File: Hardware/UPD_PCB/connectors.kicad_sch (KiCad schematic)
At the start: 23 parts, among them J1 Screw_Terminal_01x02, J10 Screw_Terminal_01x02, J2 Screw_Terminal_01x02, J3 Screw_Terminal_01x02, J4 Screw_Terminal_01x02, J5 Screw_Terminal_01x02, J6 Screw_Terminal_01x02, J7 Screw_Terminal_01x02, J8 Screw_Terminal_01x02, J9 Screw_Terminal_01x02

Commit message: Updated design
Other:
- moved on the sheet: J3, J4
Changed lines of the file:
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@@
 	(wire
 		(pts
-			(xy 63.5 45.72) (xy 69.85 45.72)
+			(xy 59.69 45.72) (xy 66.04 45.72)
 		)
 		(stroke
@@
 	(wire
 		(pts
-			(xy 63.5 62.23) (xy 66.04 62.23)
+			(xy 59.69 62.23) (xy 62.23 62.23)
 		)
 		(stroke
@@
 	(wire
 		(pts
-			(xy 63.5 59.69) (xy 66.04 59.69)
+			(xy 59.69 59.69) (xy 62.23 59.69)
 		)
 		(stroke
@@
 	(wire
 		(pts
-			(xy 66.04 48.26) (xy 63.5 48.26)
+			(xy 62.23 48.26) (xy 59.69 48.26)
 		)
 		(stroke
@@
 	)
 	(label "IP+"
-		(at 69.85 45.72 180)
+		(at 66.04 45.72 180)
 		(fields_autoplaced yes)
 		(effects
@@
 	(symbol
 		(lib_id "Connector:Screw_Terminal_01x02")
-		(at 58.42 62.23 180)
+		(at 54.61 62.23 180)
 		(unit 1)
 		(exclude_from_sim no)
@@
 		(dnp no)
 		(property "Reference" "J4"
-			(at 56.388 62.484 0)
+			(at 52.578 62.484 0)
 			(effects
 				(font
@@
 		)
 		(property "Value" "Screw_Terminal_01x02"
-			(at 56.388 59.944 0)
+			(at 52.578 59.944 0)
 			(effects
 				(font
@@
 		)
 		(property "Footprint" ""
-			(at 58.42 62.23 0)
+			(at 54.61 62.23 0)
 			(effects
 				(font
@@
 		)
 		(property "Datasheet" "~"
-			(at 58.42 62.23 0)
+			(at 54.61 62.23 0)
 			(effects
 				(font
@@
 		)
 		(property "Description" "Generic screw terminal, single row, 01x02, script generated (kicad-library-utils/schlib/autogen/connector/)"
-			(at 58.42 62.23 0)
+			(at 54.61 62.23 0)
 			(effects
 				(font
@@
 	(symbol
 		(lib_id "power:GND")
-		(at 66.04 62.23 0)
+		(at 62.23 62.23 0)
 		(unit 1)
 		(exclude_from_sim no)
@@
 		(fields_autoplaced yes)
 		(property "Reference" "#PWR058"
-			(at 66.04 68.58 0)
+			(at 62.23 68.58 0)
 			(effects
 				(font
@@
 		)
 		(property "Value" "GND"
-			(at 66.04 67.31 0)
+			(at 62.23 67.31 0)
 			(effects
 				(font
@@
 		)
 		(property "Footprint" ""
-			(at 66.04 62.23 0)
+			(at 62.23 62.23 0)
 			(effects
 				(font
@@
 		)
 		(property "Datasheet" ""
-			(at 66.04 62.23 0)
+			(at 62.23 62.23 0)
 			(effects
 				(font
@@
 		)
 		(property "Description" "Power symbol creates a global label with name \"GND\" , ground"
-			(at 66.04 62.23 0)
+			(at 62.23 62.23 0)
 			(effects
 				(font
@@
 	(symbol
 		(lib_id "power:GND")
-		(at 66.04 48.26 0)
+		(at 62.23 48.26 0)
 		(unit 1)
 		(exclude_from_sim no)
@@
 		(fields_autoplaced yes)
 		(property "Reference" "#PWR056"
-			(at 66.04 54.61 0)
+			(at 62.23 54.61 0)
 			(effects
 				(font
@@
 		)
 		(property "Value" "GND"
-			(at 66.04 53.34 0)
+			(at 62.23 53.34 0)
 			(effects
 				(font
@@
 		)
 		(property "Footprint" ""
-			(at 66.04 48.26 0)
+			(at 62.23 48.26 0)
 			(effects
 				(font
@@
 		)
 		(property "Datasheet" ""
-			(at 66.04 48.26 0)
+			(at 62.23 48.26 0)
 			(effects
 				(font
@@
 		)
 		(property "Description" "Power symbol creates a global label with name \"GND\" , ground"
-			(at 66.04 48.26 0)
+			(at 62.23 48.26 0)
 			(effects
 				(font
@@
 	(symbol
 		(lib_id "Connector:Screw_Terminal_01x02")
-		(at 58.42 48.26 180)
+		(at 54.61 48.26 180)
 		(unit 1)
 		(exclude_from_sim no)
@@
 		(dnp no)
 		(property "Reference" "J3"
-			(at 56.388 48.514 0)
+			(at 52.578 48.514 0)
 			(effects
 				(font
@@
 		)
 		(property "Value" "Screw_Terminal_01x02"
-			(at 56.388 45.974 0)
+			(at 52.578 45.974 0)
 			(effects
 				(font
@@
 		)
 		(property "Footprint" ""
-			(at 58.42 48.26 0)
+			(at 54.61 48.26 0)
 			(effects
 				(font
@@
 		)
 		(property "Datasheet" "~"
-			(at 58.42 48.26 0)
+			(at 54.61 48.26 0)
 			(effects
 				(font
@@
 		)
 		(property "Description" "Generic screw terminal, single row, 01x02, script generated (kicad-library-utils/schlib/autogen/connector/)"
-			(at 58.42 48.26 0)
+			(at 54.61 48.26 0)
 			(effects
 				(font
@@
 	(symbol
 		(lib_id "power:+5V")
-		(at 66.04 59.69 270)
+		(at 62.23 59.69 270)
 		(unit 1)
 		(exclude_from_sim no)
@@
 		(fields_autoplaced yes)
 		(property "Reference" "#PWR057"
+			(at 58.42 59.69 0)
+			(effects
+				(font
+					(size 1.27 1.27)
+				)
+				(hide yes)
+			)
+		)
+		(property "Value" "+5V"
+			(at 66.04 59.6899 90)
+			(effects
+				(font
+					(size 1.27 1.27)
+				)
+				(justify left)
+			)
+		)
+		(property "Footprint" ""
 			(at 62.23 59.69 0)
 			(effects
@@
 			)
 		)
-		(property "Value" "+5V"
-			(at 69.85 59.6899 90)
-			(effects
-				(font
-					(size 1.27 1.27)
-				)
-				(justify left)
-			)
-		)
-		(property "Footprint" ""
-			(at 66.04 59.69 0)
-			(effects
-				(font
-					(size 1.27 1.27)
-				)
-				(hide yes)
-			)
-		)
 		(property "Datasheet" ""
-			(at 66.04 59.69 0)
+			(at 62.23 59.69 0)
 			(effects
 				(font
@@
 		)
 		(property "Description" "Power symbol creates a global label with name \"+5V\""
-			(at 66.04 59.69 0)
-			(effects
-				(font
+			(at 62.23 59.69 0)
+			(effects
+				(font

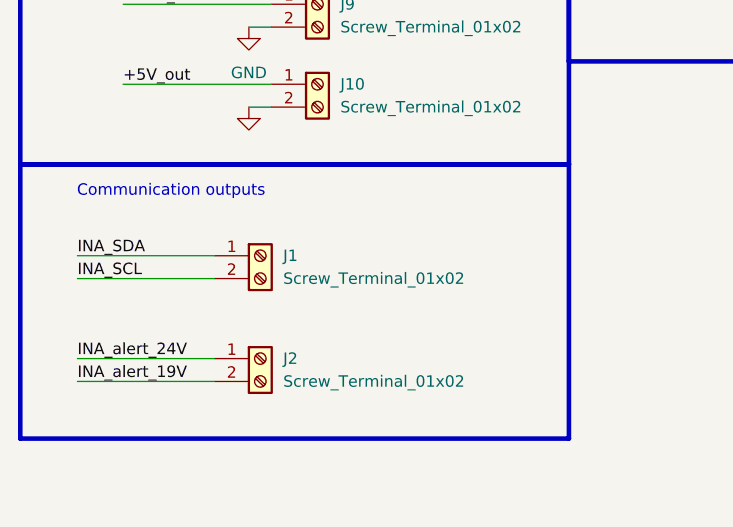
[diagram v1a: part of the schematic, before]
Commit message: Updated schematic (before INA219 integration)
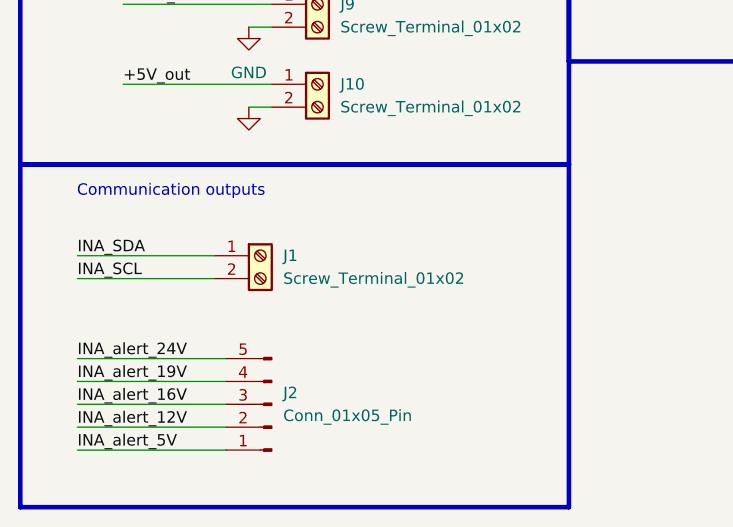
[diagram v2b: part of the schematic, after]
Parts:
- removed J2: Screw_Terminal_01x02, symbol Connector:Screw_Terminal_01x02
- added J2: Conn_01x05_Pin, Connector_PinHeader_1.00mm:PinHeader_1x05_P1.00mm_Vertical, symbol Connector:Conn_01x05_Pin
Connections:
- net INA_alert_19V: now also J2.4 (Pin_4)
- net INA_alert_24V: now also J2.5 (Pin_5)
- new net INA_alert_12V: J2.2 (Pin_2)
- new net INA_alert_16V: J2.3 (Pin_3)
- new net INA_alert_5V: J2.1 (Pin_1)
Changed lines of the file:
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@@
+	(wire
+		(pts
+			(xy 33.02 166.37) (xy 49.53 166.37)
+		)
+		(stroke
+			(width 0)
+			(type default)
+		)
+	)
 	(wire
 		(pts
@@
 	(wire
 		(pts
-			(xy 33.02 158.75) (xy 48.26 158.75)
+			(xy 33.02 158.75) (xy 49.53 158.75)
+		)
+		(stroke
+			(width 0)
+			(type default)
+		)
+	)
+	(wire
+		(pts
+			(xy 33.02 163.83) (xy 49.53 163.83)
 		)
 		(stroke
@@
 	(wire
 		(pts
-			(xy 33.02 161.29) (xy 48.26 161.29)
+			(xy 33.02 161.29) (xy 49.53 161.29)
 		)
 		(stroke
@@
 		(pts
 			(xy 93.98 43.18) (xy 104.14 43.18)
+		)
+		(stroke
+			(width 0)
+			(type default)
+		)
+	)
+	(wire
+		(pts
+			(xy 33.02 168.91) (xy 49.53 168.91)
 		)
 		(stroke
@@
 	(rectangle
 		(start 26.67 137.16)
-		(end 87.63 167.64)
+		(end 87.63 175.26)
 		(stroke
 			(width 0.508)
@@
 		)
 	)
+	(label "INA_alert_5V"
+		(at 33.02 168.91 0)
+		(fields_autoplaced yes)
+		(effects
+			(font
+				(size 1.27 1.27)
+			)
+			(justify left bottom)
+		)
+	)
 	(label "INA_SDA"
 		(at 33.02 147.32 0)
@@
 		)
 	)
+	(label "INA_alert_12V"
+		(at 33.02 166.37 0)
+		(fields_autoplaced yes)
+		(effects
+			(font
+				(size 1.27 1.27)
+			)
+			(justify left bottom)
+		)
+	)
 	(label "+12V_out"
 		(at 93.98 91.44 0)
@@
 		)
 	)
+	(label "INA_alert_16V"
+		(at 33.02 163.83 0)
+		(fields_autoplaced yes)
+		(effects
+			(font
+				(size 1.27 1.27)
+			)
+			(justify left bottom)
+		)
+	)
 	(label "IP+"
 		(at 66.04 45.72 180)
@@
 	)
 	(symbol
-		(lib_id "Connector:Screw_Terminal_01x02")
-		(at 53.34 158.75 0)
-		(unit 1)
-		(exclude_from_sim no)
-		(in_bom yes)
-		(on_board yes)
-		(dnp no)
-		(fields_autoplaced yes)
-		(property "Reference" "J2"
-			(at 55.88 158.7499 0)
-			(effects
-				(font
-					(size 1.27 1.27)
-				)
-				(justify left)
-			)
-		)
-		(property "Value" "Screw_Terminal_01x02"
-			(at 55.88 161.2899 0)
-			(effects
-				(font
-					(size 1.27 1.27)
-				)
-				(justify left)
-			)
-		)
-		(property "Footprint" ""
-			(at 53.34 158.75 0)
-			(effects
-				(font
-					(size 1.27 1.27)
-				)
-				(hide yes)
-			)
-		)
-		(property "Datasheet" "~"
-			(at 53.34 158.75 0)
-			(effects
-				(font
-					(size 1.27 1.27)
-				)
-				(hide yes)
-			)
-		)
-		(property "Description" "Generic screw terminal, single row, 01x02, script generated (kicad-library-utils/schlib/autogen/connector/)"
-			(at 53.34 158.75 0)
-			(effects
-				(font
-					(size 1.27 1.27)
-				)
-				(hide yes)
-			)
-		)
-		(pin "2"
-		)
-		(pin "1"
-		)
-		(instances
-			(project "UPD_PCB"
-				(path "/0650c7a8-acba-429c-9f8e-eec0baf0bc1c/fede4c36-00cc-4d3d-b71c-5243ba232202/7d5a1283-086b-46b0-8df7-a9850521fb5e/4a3b49c6-ce69-4997-95b2-b7bb4e96c397"
-					(reference "J2")
-					(unit 1)
-				)
-			)
-		)
-	)
-	(symbol
 		(lib_id "Device:LED")
 		(at 107.95 80.01 180)
@@
 					(unit 1)
 				)
+			)
+		)
+	)
+	(symbol
+		(lib_id "Connector:Conn_01x05_Pin")
+		(at 54.61 163.83 180)
+		(unit 1)
+		(exclude_from_sim no)
+		(in_bom yes)
+		(on_board yes)
+		(dnp no)
+		(fields_autoplaced yes)
+		(property "Reference" "J2"
+			(at 55.88 162.5599 0)
+			(effects
+				(font
+					(size 1.27 1.27)
+				)
+				(justify right)
+			)
+		)
+		(property "Value" "Conn_01x05_Pin"
+			(at 55.88 165.0999 0)
+			(effects
+				(font
+					(size 1.27 1.27)
+				)
+				(justify right)
+			)
+		)
+		(property "Footprint" "Connector_PinHeader_1.00mm:PinHeader_1x05_P1.00mm_Vertical"
+			(at 54.61 163.83 0)
+			(effects
+				(font
+					(size 1.27 1.27)
+				)
+				(hide yes)
+			)
+		)
+		(property "Datasheet" "~"
+			(at 54.61 163.83 0)
+			(effects
+				(font
+					(size 1.27 1.27)
+				)
+				(hide yes)
+			)
+		)
+		(property "Description" "Generic connector, single row, 01x05, script generated"
+			(at 54.61 163.83 0)
+			(effects
+				(font
+					(size 1.27 1.27)
+				)
+				(hide yes)
+			)
+		)
+		(pin "1"
+		)
+		(pin "4"
+		)
+		(pin "3"
+		)
+		(pin "2"
+		)
+		(pin "5"
+		)
+		(instances
+			(project ""
+				(path "/0650c7a8-acba-429c-9f8e-eec0baf0bc1c/fede4c36-00cc-4d3d-b71c-5243ba232202/7d5a1283-086b-46b0-8df7-a9850521fb5e/4a3b49c6-ce69-4997-95b2-b7bb4e96c397"
+					(reference "J2")
+					(unit 1)
+				)

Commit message: Finalized Schematic
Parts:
- removed F1: Fuse, symbol Device:Fuse
- removed J1: Screw_Terminal_01x02, symbol Connector:Screw_Terminal_01x02
- removed J2: Conn_01x05_Pin, Connector_PinHeader_1.00mm:PinHeader_1x05_P1.00mm_Vertical, symbol Connector:Conn_01x05_Pin
- added D8: LED, LED_SMD:LED_0603_1608Metric_Pad1.05x0.95mm_HandSolder, symbol Device:LED
- added J1: 25A Fuse holder, 3557-2, symbol 3557-2:3557-2
- added J11, J12: Conn_01x02, Connector_PinHeader_1.00mm:PinHeader_1x02_P1.00mm_Vertical, symbol Connector_Generic:Conn_01x02
- added J2: Screw_Terminal_01x02, TerminalBlock_Philmore:TerminalBlock_Philmore_TB132_1x02_P5.00mm_Horizontal, symbol Connector:Screw_Terminal_01x02
- added R52: 330, Resistor_SMD:R_0603_1608Metric_Pad0.98x0.95mm_HandSolder, symbol Device:R
- D5: footprint Resistor_SMD:R_0603_1608Metric_Pad0.98x0.95mm_HandSolder -> LED_SMD:LED_0603_1608Metric_Pad1.05x0.95mm_HandSolder
- J10, J3, J4, J5, J6, J7, J8, J9: footprint (none) -> TerminalBlock_Philmore:TerminalBlock_Philmore_TB132_1x02_P5.00mm_Horizontal
- renumbered R38 to R46, R39 to R47, R40 to R48, R41 to R49, R42 to R50, R43 to R51
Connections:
- net +16V_out: now also J6.1 (Pin_1); no longer J8.1 (Pin_1)
- net +19V_out: now also J5.1 (Pin_1); no longer J7.1 (Pin_1)
- net +24V_out: now also J4.1 (Pin_1); no longer J6.1 (Pin_1)
- net +5V: now also J3.2 (Pin_2); no longer J4.2 (Pin_2)
- net +5V_out: now also J9.1 (Pin_1), D8.2 (A); no longer D7.2 (A), J10.1 (Pin_1)
- net GND: now also J4.2 (Pin_2), J2.1 (Pin_1), R52.1; no longer J4.1 (Pin_1)
- net INA_SCL: now also J11.2 (Pin_2)
- net INA_SDA: now also J11.1 (Pin_1)
- net IP+: now also J2.2 (Pin_2); no longer J3.2 (Pin_2)
- net +12V_out renamed +12V_1_out
- net +12V_1_out: now also J7.1 (Pin_1); no longer J9.1 (Pin_1)
- new net: J1.2, J1.4, J10.1 (Pin_1)
- new net: D8.1 (K), R52.2
- new net +12V_2_out: D7.2 (A), J8.1 (Pin_1)
- new net +42V: J1.1, J1.3
- new net VIOUT: J12.1 (Pin_1)
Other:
- moved on the sheet: D2, D3, D4, D6, D7, R46, R47, R48, R49, R50, R51

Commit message: First board layout
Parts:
- removed J10, J2, J3, J4, J5, J6, J7, J8, J9: Screw_Terminal_01x02, TerminalBlock_Philmore:TerminalBlock_Philmore_TB132_1x02_P5.00mm_Horizontal, symbol Connector:Screw_Terminal_01x02
- removed J12: Conn_01x02, Connector_PinHeader_1.00mm:PinHeader_1x02_P1.00mm_Vertical, symbol Connector_Generic:Conn_01x02
- added J10, J2: 796739-2, 7967392, symbol 796739-2:796739-2
- added J12: Conn_01x01, Connector_PinHeader_1.00mm:PinHeader_1x01_P1.00mm_Vertical, symbol Connector_Generic:Conn_01x01
- added J3: Conn_01x02, Connector_PinHeader_1.00mm:PinHeader_1x02_P1.00mm_Vertical, symbol Connector_Generic:Conn_01x02
- added J4, J5, J6, J7, J8: 1776119-2, 17761192, symbol 1776119-2:1776119-2
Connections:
- net +12V_1_out: now also J6.1
- net +12V_2_out: now also J7.1
- net +16V_out: now also J5.1
- net +19V_out: now also J4.1
- net +5V: now also J3.2 (Pin_2)
- net +5V_out: now also J8.1
- net GND: now also J10.2, J2.1, J3.1 (Pin_1), J4.2, J5.2, J6.2, J7.2, J8.2
- net IP+: now also J2.2
- net VIOUT: now also J12.1 (Pin_1)
- net at J1.2, J1.4: now also J10.1

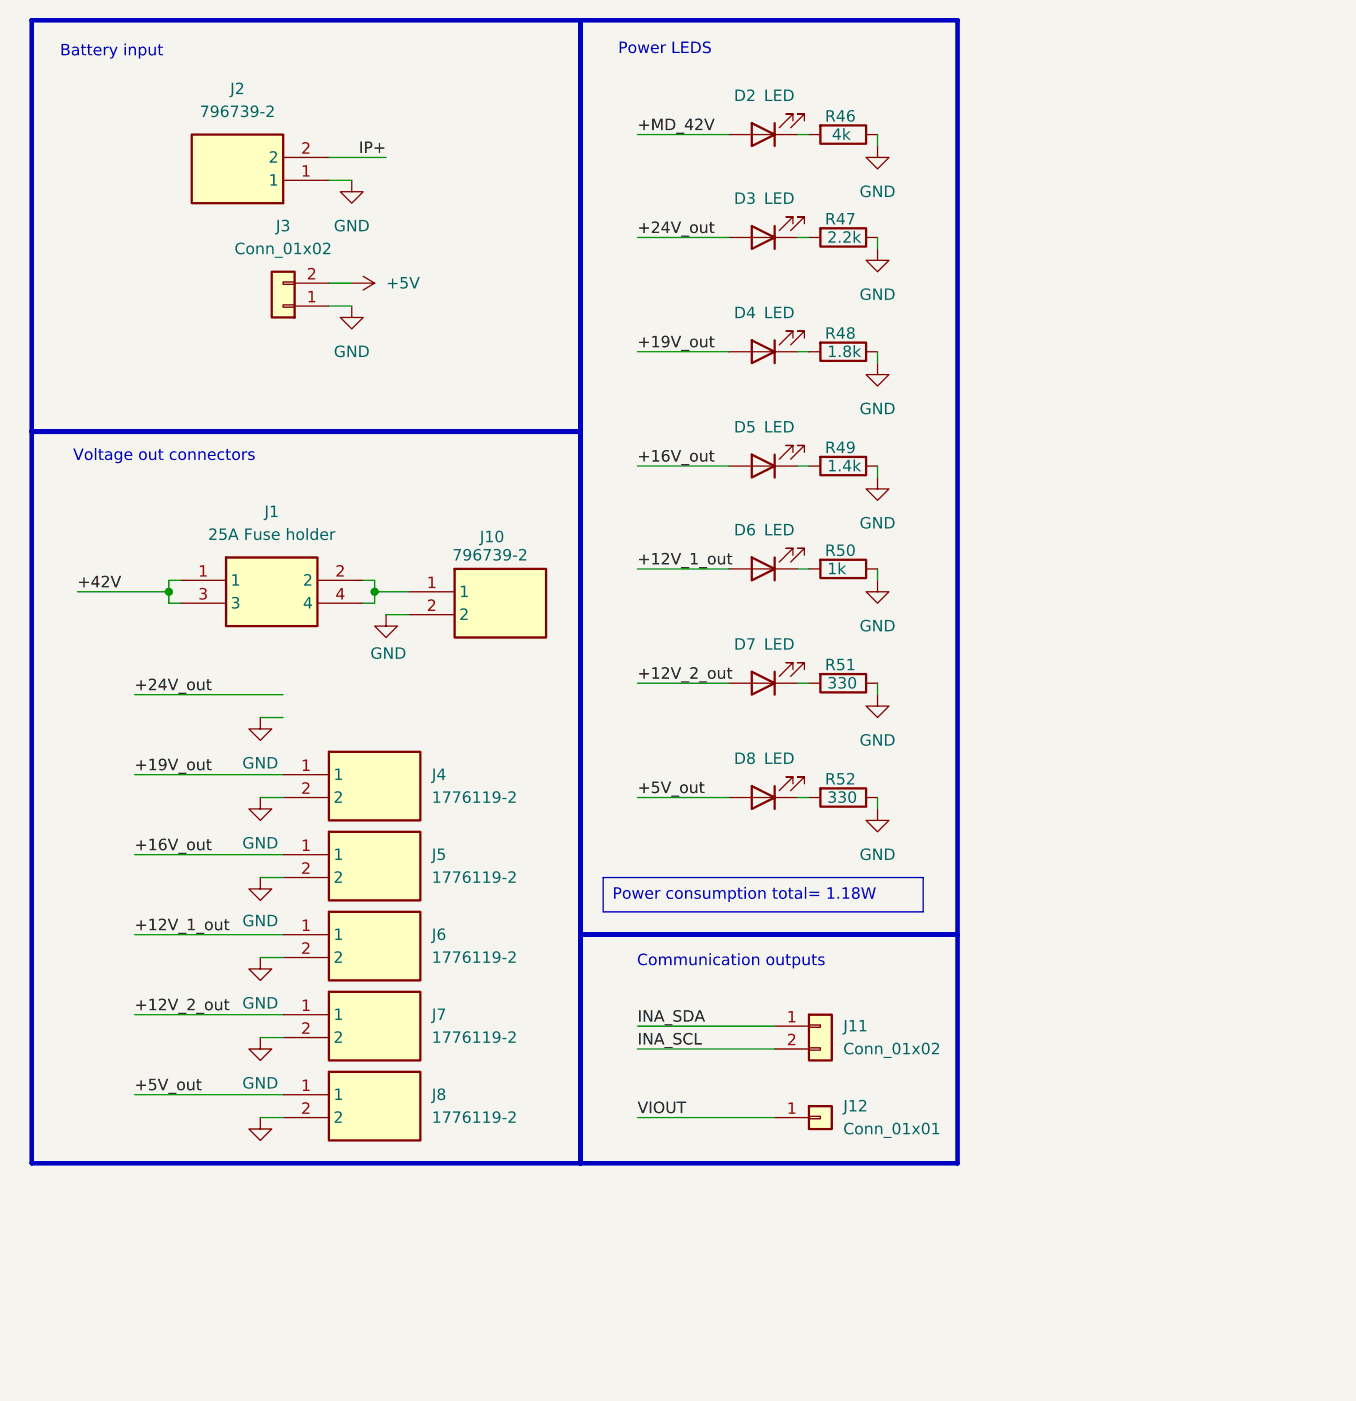
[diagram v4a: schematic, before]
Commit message: Pcb layout before changing inductor
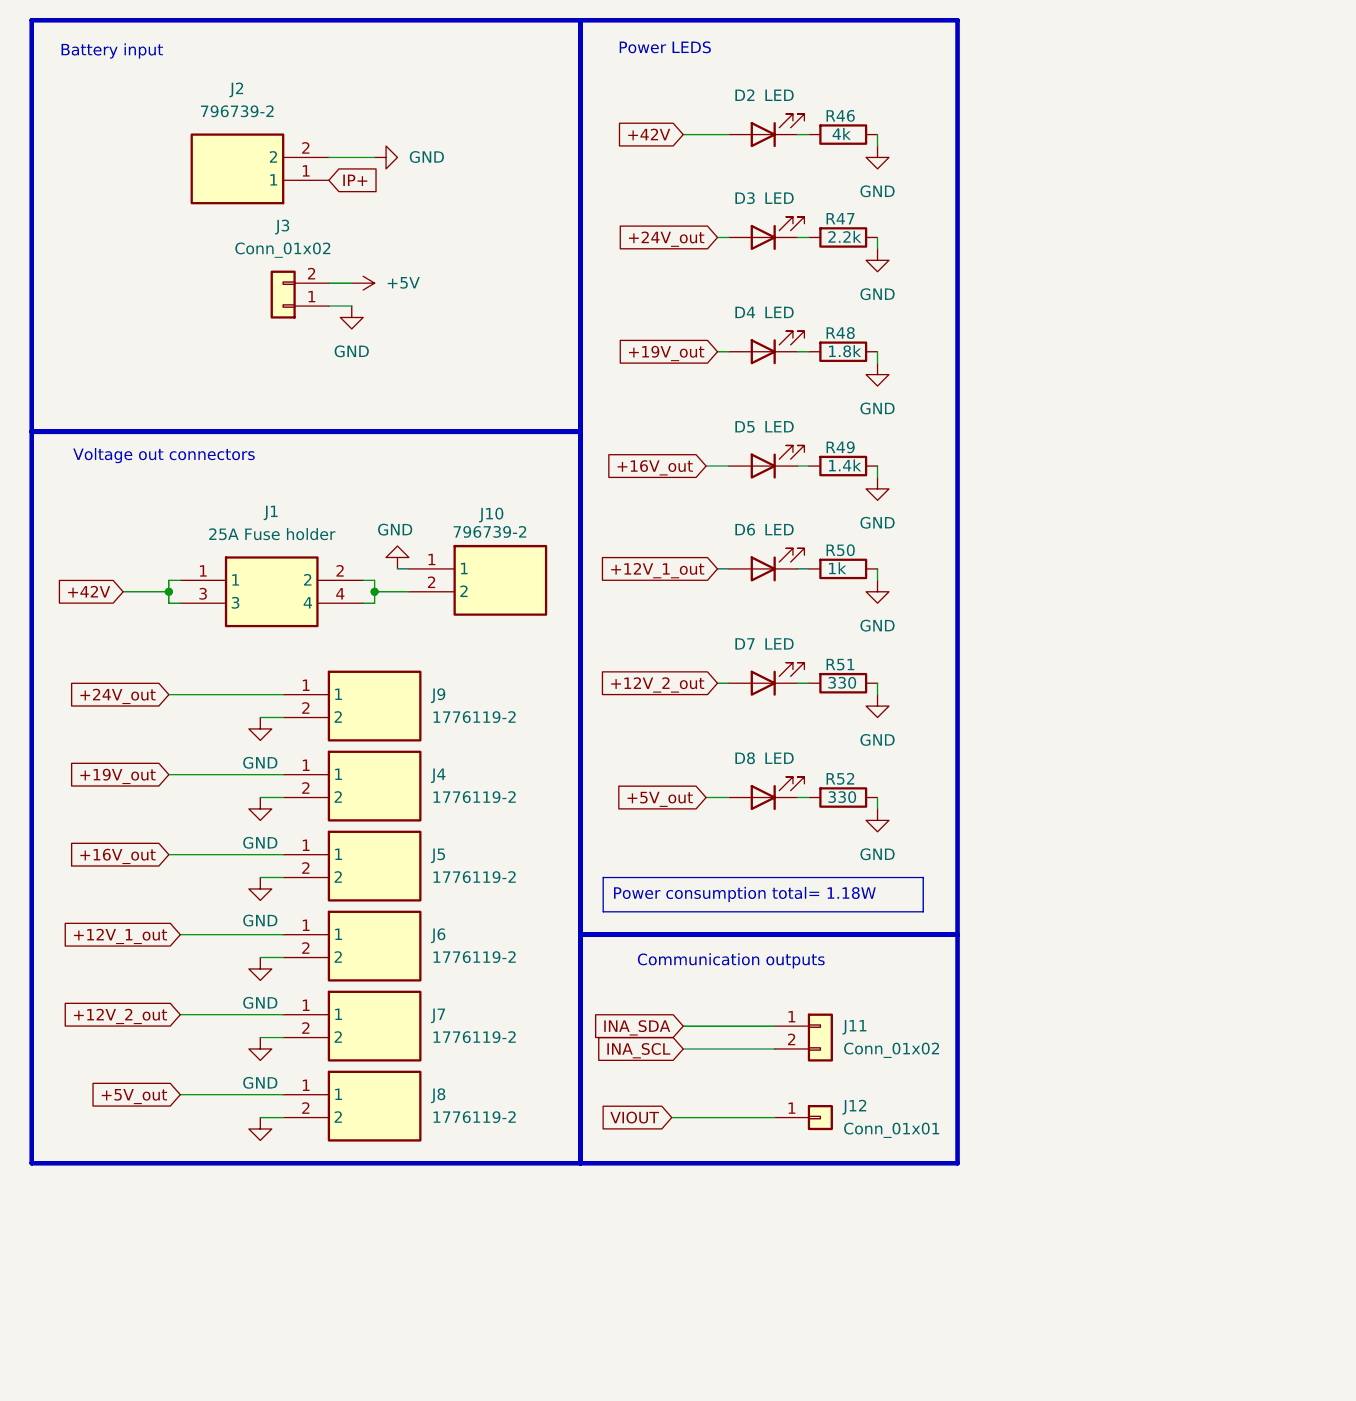
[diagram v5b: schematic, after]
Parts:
- added J9: 1776119-2, 17761192, symbol 1776119-2:1776119-2
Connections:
- net +MD_42V is gone; now on net +42V: D2.2 (A)
- net +24V_out: now also J9.1
- net GND: now also J10.1, J2.2, J9.2; no longer J10.2, J2.1
- net IP+: now also J2.1; no longer J2.2
- net at J1.2, J1.4: now also J10.2; no longer J10.1
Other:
- moved on the sheet: J10
